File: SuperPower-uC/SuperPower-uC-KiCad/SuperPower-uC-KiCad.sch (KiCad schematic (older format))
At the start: 0 parts

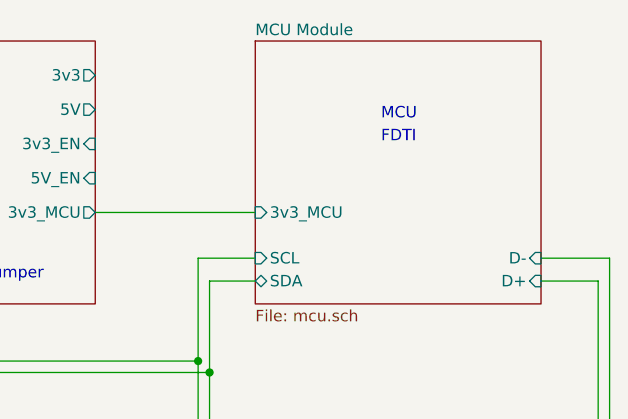
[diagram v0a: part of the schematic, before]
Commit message: Fixed FTDI misspelling
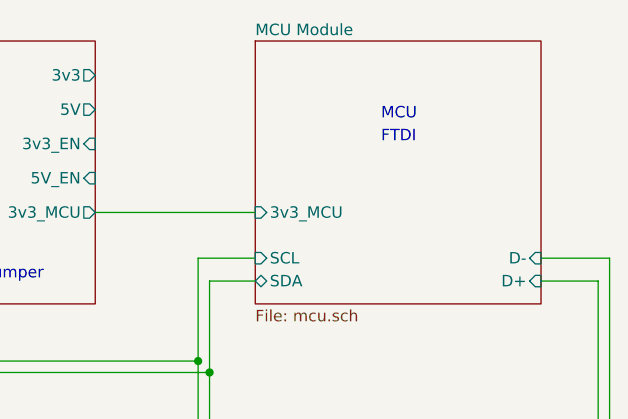
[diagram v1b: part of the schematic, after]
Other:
- note added: "FTDI"
- note removed: "FDTI"
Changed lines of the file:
@@
 Permanent Power Jumper
 Text Notes 7400 2550 0    50   ~ 0
-FDTI
+FTDI
 Text Notes 5350 4650 0    50   ~ 0
 Bypass Jumper
